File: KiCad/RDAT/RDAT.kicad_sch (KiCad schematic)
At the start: 16 parts

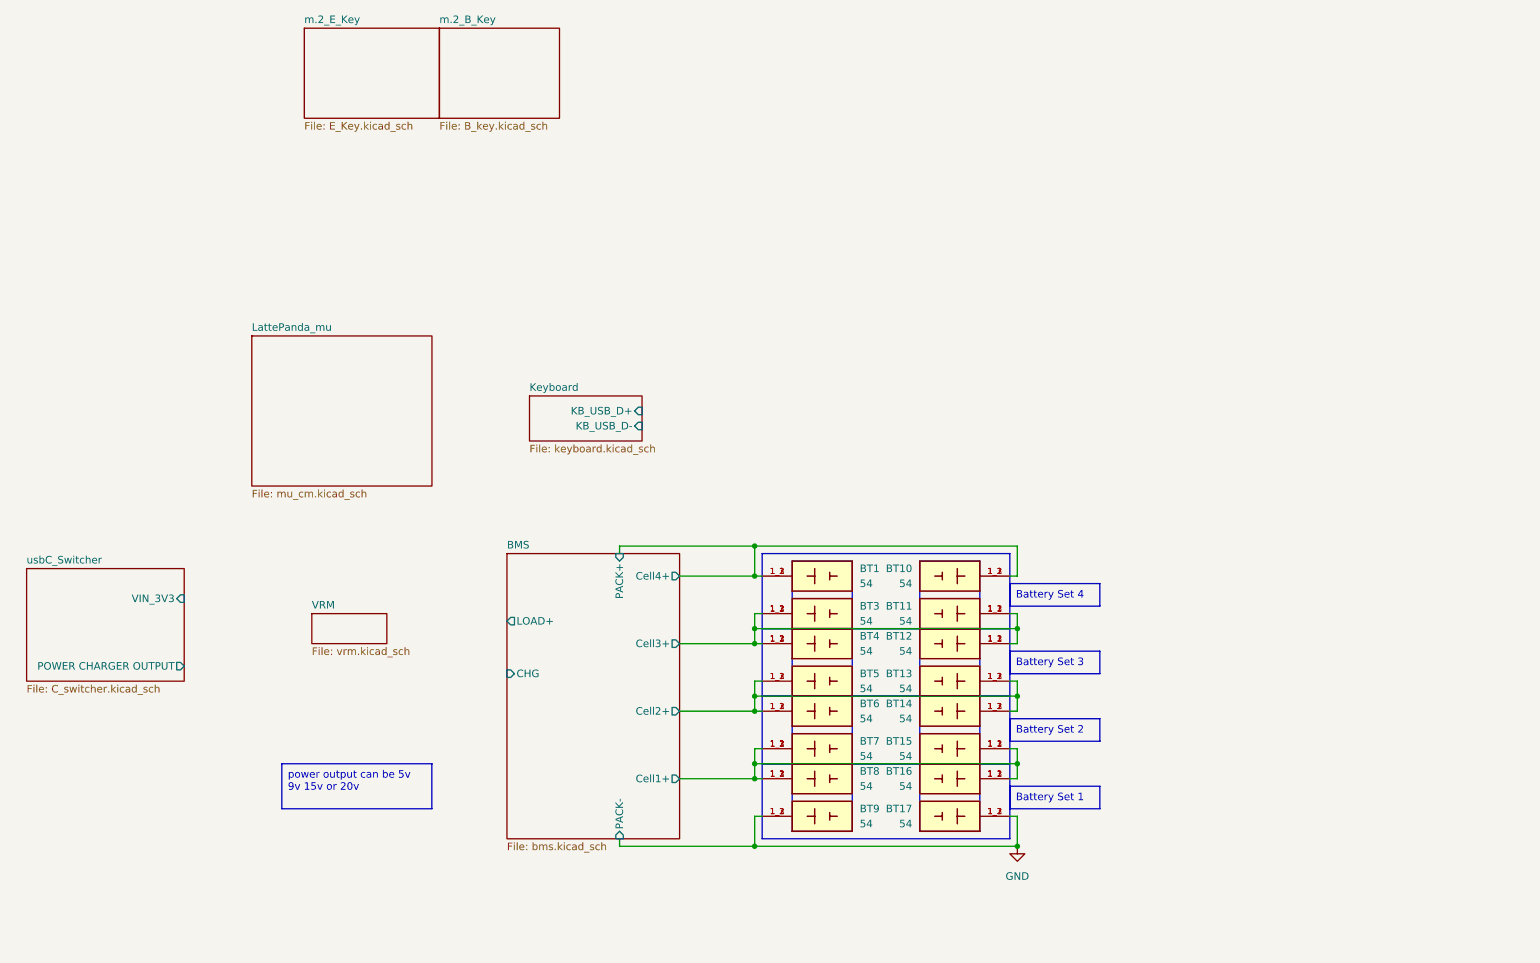
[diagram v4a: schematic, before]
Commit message: Add new notes; update component references in schematics and footprints, and complete charging design
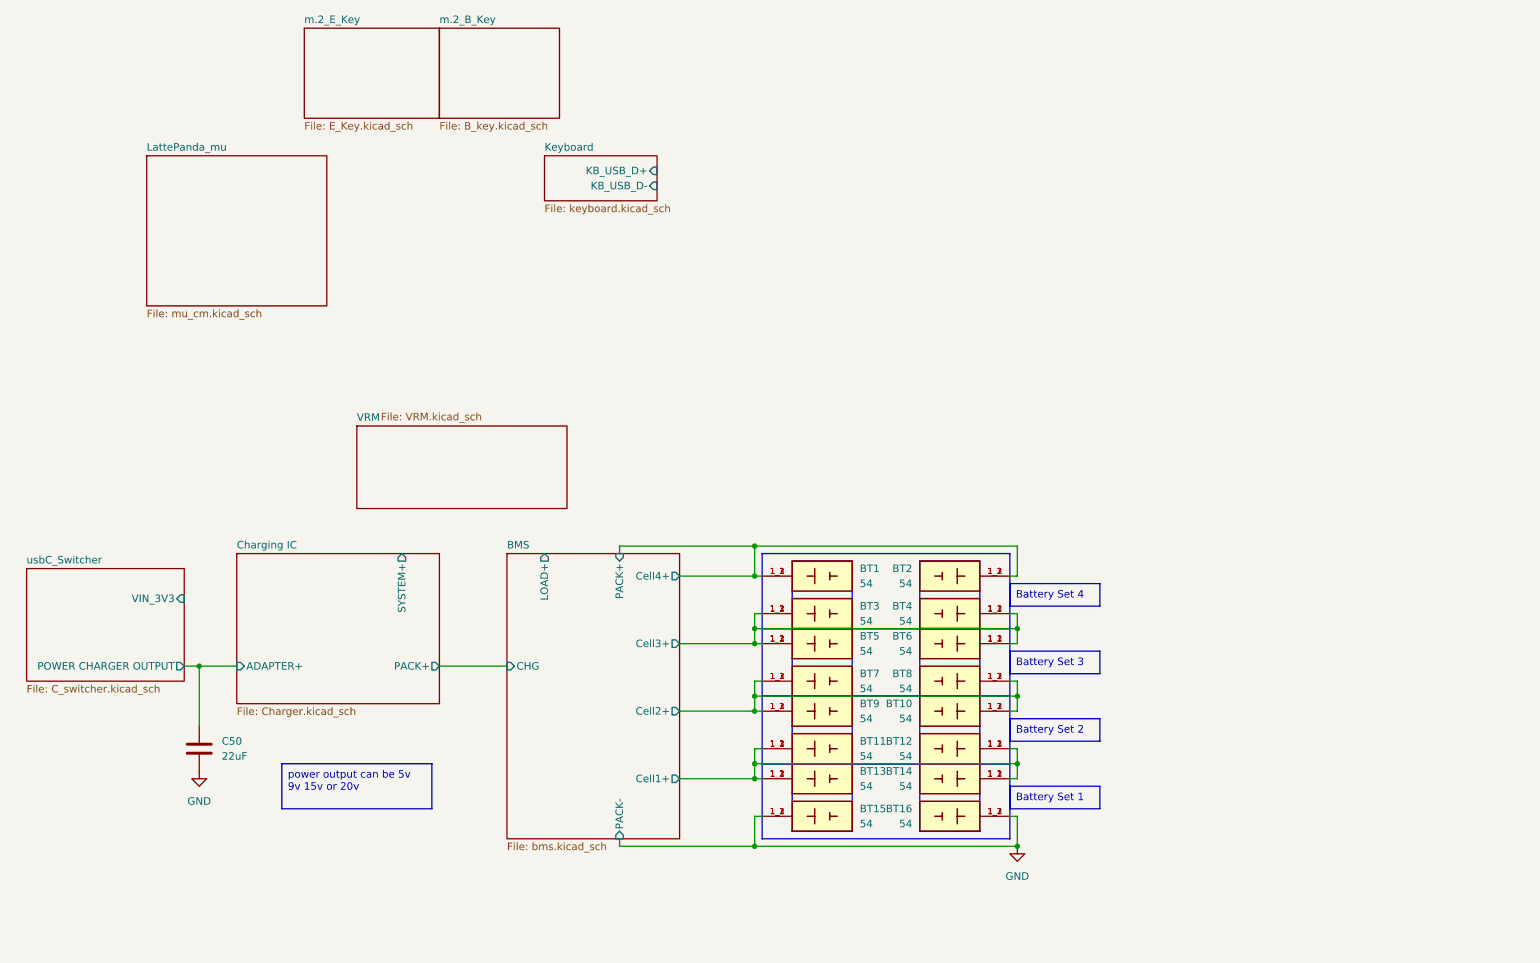
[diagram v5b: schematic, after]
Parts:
- added C50: 22uF, symbol Device:C
- renumbered BT14 to BT10, BT7 to BT11, BT15 to BT12, BT8 to BT13, BT16 to BT14, BT9 to BT15, BT17 to BT16, BT10 to BT2, BT11 to BT4, BT4 to BT5, BT12 to BT6, BT5 to BT7, BT13 to BT8, BT6 to BT9
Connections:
- net GND: now also C50.2
- new net Charging IC/ADAPTER+: C50.1
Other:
- added sheet Charging IC (Charger.kicad_sch)
- sheet VRM: file vrm.kicad_sch -> VRM.kicad_sch

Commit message: Update VRM stuff
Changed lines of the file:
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@@
 		)
 	)
-	(text_box "power output can be 5v 9v 15v or 20v"
+	(text_box "4S2P\nV_{nominal} = 14.4V\nV_{charged} = 16.8V\nV_{discharged} = 10V"
 		(exclude_from_sim no)
-		(at 60.96 153.67 0)
-		(size 25.4 7.62)
+		(at 100.33 171.45 0)
+		(size 64.77 13.97)
 		(margins 0.9525 0.9525 0.9525 0.9525)
 		(stroke
 			(width 0)
-			(type default)
+			(type solid)
 		)
 		(fill
+			(type none)
+		)
+		(effects
+			(font
+				(size 1.27 1.27)
+			)
+			(justify left top)
+		)
+	)
+	(text_box "power output can be \n5v 9v 15v or 20v /3A\nwith 100W:\n20v /3A\nwith 240W:\n28v 36v 48v /5A"
+		(exclude_from_sim no)
+		(at 60.96 153.67 0)
+		(size 25.4 13.97)
+		(margins 0.9525 0.9525 0.9525 0.9525)
+		(stroke
+			(width 0)
+			(type solid)
+		)
+		(fill

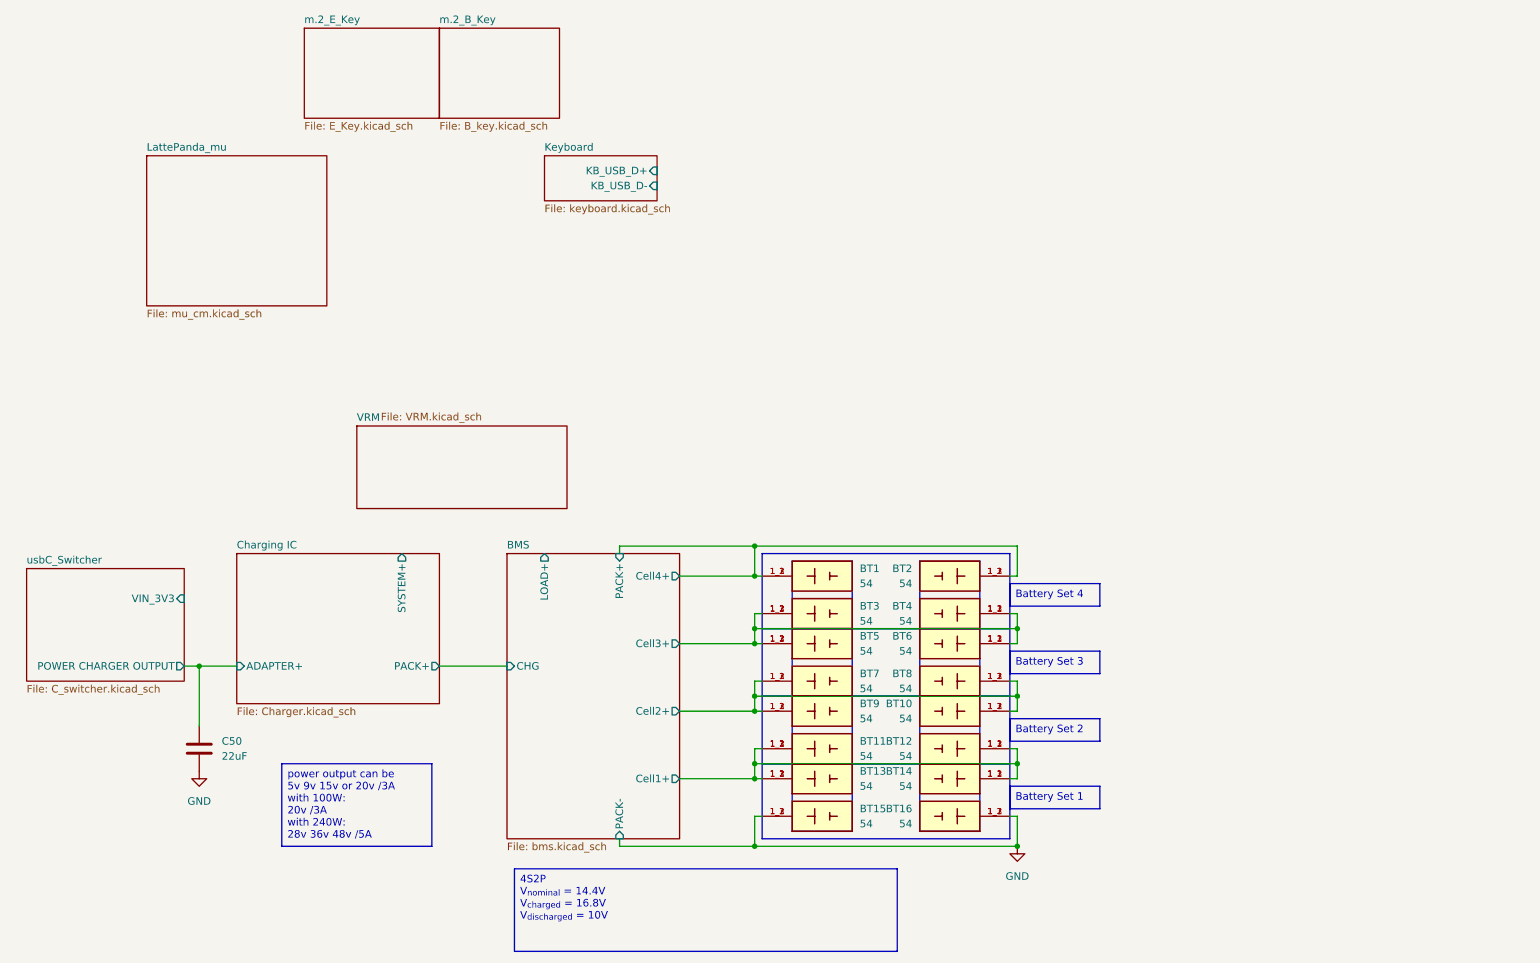
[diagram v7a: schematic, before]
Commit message: Added example and updated power path
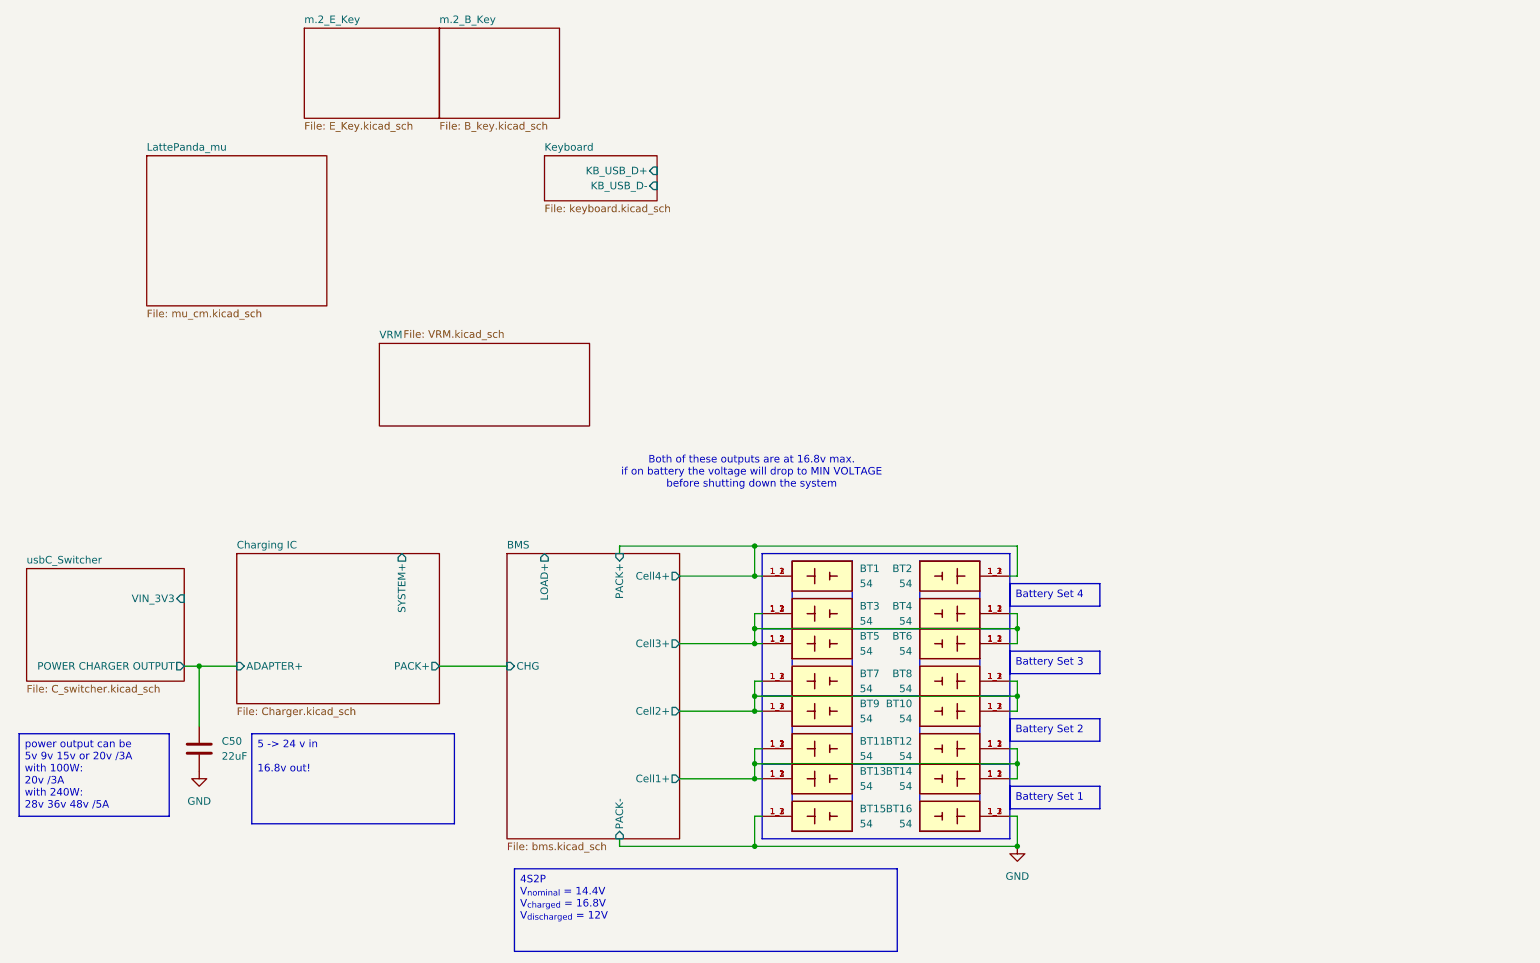
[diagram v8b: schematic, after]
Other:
- note added: "Both of these outputs are at 16.8v max. if on battery the voltage will drop to MIN VOLTAGE before shutting down the system"
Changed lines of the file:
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@@
 		)
 	)
+	(text "Both of these outputs are at 16.8v max.\nif on battery the voltage will drop to MIN VOLTAGE\nbefore shutting down the system\n"
+		(exclude_from_sim no)
+		(at 140.462 104.394 0)
+		(effects
+			(font
+				(size 1.27 1.27)
+			)
+		)
+	)
 	(text_box "Battery Set 2\n"
 		(exclude_from_sim no)
@@
 		)
 	)
-	(text_box "4S2P\nV_{nominal} = 14.4V\nV_{charged} = 16.8V\nV_{discharged} = 10V"
+	(text_box "5 -> 24 v in\n\n16.8v out!\n"
+		(exclude_from_sim no)
+		(at 55.88 148.59 0)
+		(size 34.29 15.24)
+		(margins 0.9525 0.9525 0.9525 0.9525)
+		(stroke
+			(width 0)
+			(type solid)
+		)
+		(fill
+			(type none)
+		)
+		(effects
+			(font
+				(size 1.27 1.27)
+			)
+			(justify left top)
+		)
+	)
+	(text_box "4S2P\nV_{nominal} = 14.4V\nV_{charged} = 16.8V\nV_{discharged} = 12V"
 		(exclude_from_sim no)
 		(at 100.33 171.45 0)
@@
 	(text_box "power output can be \n5v 9v 15v or 20v /3A\nwith 100W:\n20v /3A\nwith 240W:\n28v 36v 48v /5A"
 		(exclude_from_sim no)
-		(at 60.96 153.67 0)
+		(at 16.51 148.59 0)
 		(size 25.4 13.97)
 		(margins 0.9525 0.9525 0.9525 0.9525)
@@
 	)
 	(sheet
-		(at 73.66 96.52)
+		(at 77.47 82.55)
 		(size 35.56 13.97)
 		(exclude_from_sim no)
@@
 		)
 		(property "Sheetname" "VRM"
-			(at 73.66 95.8084 0)
+			(at 77.47 81.8384 0)
 			(effects
 				(font
@@
 		)
 		(property "Sheetfile" "VRM.kicad_sch"
-			(at 77.724 94.234 0)
+			(at 81.534 80.264 0)
 			(effects
 				(font
